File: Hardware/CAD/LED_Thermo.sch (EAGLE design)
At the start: 41 parts, among them IC1 MEGA48/88/168-AU, IC2 MAX481CSA, J1 USB_Micro, Q2 KERAMIKRESONATOR_CSTCC_16MHZ

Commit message: Sicherung eingefuegt, Gerberdateien aktualisiert
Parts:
- added F1: FUSE, fuse:FUSE
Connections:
- new net N$4: F1.1, J1.VBUS
- net VCC: now also F1.2; no longer J1.VBUS
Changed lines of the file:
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@@
 <setting verticaltext="up"/>
 </settings>
-<grid distance="25" unitdist="mil" unit="mil" style="lines" multiple="1" display="no" altdistance="5" altunitdist="mil" altunit="mil"/>
+<grid distance="50" unitdist="mil" unit="mil" style="lines" multiple="1" display="no" altdistance="5" altunitdist="mil" altunit="mil"/>
 <layers>
-<layer number="1" name="Top" color="4" fill="1" visible="yes" active="no"/>
-<layer number="2" name="Route2" color="1" fill="3" visible="yes" active="no"/>
-<layer number="3" name="Route3" color="4" fill="3" visible="yes" active="no"/>
-<layer number="4" name="Route4" color="1" fill="4" visible="yes" active="no"/>
-<layer number="5" name="Route5" color="4" fill="4" visible="yes" active="no"/>
-<layer number="6" name="Route6" color="1" fill="8" visible="yes" active="no"/>
-<layer number="7" name="Route7" color="4" fill="8" visible="yes" active="no"/>
-<layer number="8" name="Route8" color="1" fill="2" visible="yes" active="no"/>
-<layer number="9" name="Route9" color="4" fill="2" visible="yes" active="no"/>
-<layer number="10" name="Route10" color="1" fill="7" visible="yes" active="no"/>
-<layer number="11" name="Route11" color="4" fill="7" visible="yes" active="no"/>
-<layer number="12" name="Route12" color="1" fill="5" visible="yes" active="no"/>
-<layer number="13" name="Route13" color="4" fill="5" visible="yes" active="no"/>
-<layer number="14" name="Route14" color="1" fill="6" visible="yes" active="no"/>
-<layer number="15" name="Route15" color="4" fill="6" visible="yes" active="no"/>
-<layer number="16" name="Bottom" color="1" fill="1" visible="yes" active="no"/>
-<layer number="17" name="Pads" color="2" fill="1" visible="yes" active="no"/>
-<layer number="18" name="Vias" color="2" fill="1" visible="yes" active="no"/>
-<layer number="19" name="Unrouted" color="6" fill="1" visible="yes" active="no"/>
-<layer number="20" name="Dimension" color="15" fill="1" visible="yes" active="no"/>
-<layer number="21" name="tPlace" color="7" fill="1" visible="yes" active="no"/>
-<layer number="22" name="bPlace" color="7" fill="1" visible="yes" active="no"/>
-<layer number="23" name="tOrigins" color="15" fill="1" visible="yes" active="no"/>
-<layer number="24" name="bOrigins" color="15" fill="1" visible="yes" active="no"/>
-<layer number="25" name="tNames" color="7" fill="1" visible="yes" active="no"/>
-<layer number="26" name="bNames" color="7" fill="1" visible="yes" active="no"/>
-<layer number="27" name="tValues" color="7" fill="1" visible="yes" active="no"/>
-<layer number="28" name="bValues" color="7" fill="1" visible="yes" active="no"/>
+<layer number="1" name="Top" color="4" fill="1" visible="no" active="no"/>
+<layer number="2" name="Route2" color="1" fill="3" visible="no" active="no"/>
+<layer number="3" name="Route3" color="4" fill="3" visible="no" active="no"/>
+<layer number="4" name="Route4" color="1" fill="4" visible="no" active="no"/>
+<layer number="5" name="Route5" color="4" fill="4" visible="no" active="no"/>
+<layer number="6" name="Route6" color="1" fill="8" visible="no" active="no"/>
+<layer number="7" name="Route7" color="4" fill="8" visible="no" active="no"/>
+<layer number="8" name="Route8" color="1" fill="2" visible="no" active="no"/>
+<layer number="9" name="Route9" color="4" fill="2" visible="no" active="no"/>
+<layer number="10" name="Route10" color="1" fill="7" visible="no" active="no"/>
+<layer number="11" name="Route11" color="4" fill="7" visible="no" active="no"/>
+<layer number="12" name="Route12" color="1" fill="5" visible="no" active="no"/>
+<layer number="13" name="Route13" color="4" fill="5" visible="no" active="no"/>
+<layer number="14" name="Route14" color="1" fill="6" visible="no" active="no"/>
+<layer number="15" name="Route15" color="4" fill="6" visible="no" active="no"/>
+<layer number="16" name="Bottom" color="1" fill="1" visible="no" active="no"/>
+<layer number="17" name="Pads" color="2" fill="1" visible="no" active="no"/>
+<layer number="18" name="Vias" color="2" fill="1" visible="no" active="no"/>
+<layer number="19" name="Unrouted" color="6" fill="1" visible="no" active="no"/>
+<layer number="20" name="Dimension" color="15" fill="1" visible="no" active="no"/>
+<layer number="21" name="tPlace" color="7" fill="1" visible="no" active="no"/>
+<layer number="22" name="bPlace" color="7" fill="1" visible="no" active="no"/>
+<layer number="23" name="tOrigins" color="15" fill="1" visible="no" active="no"/>
+<layer number="24" name="bOrigins" color="15" fill="1" visible="no" active="no"/>
+<layer number="25" name="tNames" color="7" fill="1" visible="no" active="no"/>
+<layer number="26" name="bNames" color="7" fill="1" visible="no" active="no"/>
+<layer number="27" name="tValues" color="7" fill="1" visible="no" active="no"/>
+<layer number="28" name="bValues" color="7" fill="1" visible="no" active="no"/>
 <layer number="29" name="tStop" color="7" fill="3" visible="no" active="no"/>
 <layer number="30" name="bStop" color="7" fill="6" visible="no" active="no"/>
@@
 <layer number="35" name="tGlue" color="7" fill="4" visible="no" active="no"/>
 <layer number="36" name="bGlue" color="7" fill="5" visible="no" active="no"/>
-<layer number="37" name="tTest" color="7" fill="1" visible="yes" active="no"/>
-<layer number="38" name="bTest" color="7" fill="1" visible="yes" active="no"/>
+<layer number="37" name="tTest" color="7" fill="1" visible="no" active="no"/>
+<layer number="38" name="bTest" color="7" fill="1" visible="no" active="no"/>
 <layer number="39" name="tKeepout" color="4" fill="11" visible="no" active="no"/>
 <layer number="40" name="bKeepout" color="1" fill="11" visible="no" active="no"/>
@@
 <layer number="44" name="Drills" color="7" fill="1" visible="no" active="no"/>
 <layer number="45" name="Holes" color="7" fill="1" visible="no" active="no"/>
-<layer number="46" name="Milling" color="3" fill="1" visible="yes" active="no"/>
-<layer number="47" name="Measures" color="7" fill="1" visible="yes" active="no"/>
-<layer number="48" name="Document" color="7" fill="1" visible="yes" active="no"/>
-<layer number="49" name="Reference" color="7" fill="1" visible="yes" active="no"/>
-<layer number="50" name="dxf" color="7" fill="1" visible="yes" active="no"/>
-<layer number="51" name="tDocu" color="7" fill="1" visible="yes" active="no"/>
-<layer number="52" name="bDocu" color="7" fill="1" visible="yes" active="no"/>
-<layer number="53" name="tGND_GNDA" color="7" fill="9" visible="yes" active="no"/>
-<layer number="54" name="bGND_GNDA" color="1" fill="9" visible="yes" active="no"/>
-<layer number="56" name="wert" color="7" fill="1" visible="yes" active="no"/>
-<layer number="59" name="Invisible" color="7" fill="1" visible="yes" active="no"/>
-<layer number="61" name="stand" color="7" fill="1" visible="yes" active="no"/>
+<layer number="46" name="Milling" color="3" fill="1" visible="no" active="no"/>
+<layer number="47" name="Measures" color="7" fill="1" visible="no" active="no"/>
+<layer number="48" name="Document" color="7" fill="1" visible="no" active="no"/>
+<layer number="49" name="Reference" color="7" fill="1" visible="no" active="no"/>
+<layer number="50" name="dxf" color="7" fill="1" visible="no" active="no"/>
+<layer number="51" name="tDocu" color="7" fill="1" visible="no" active="no"/>
+<layer number="52" name="bDocu" color="7" fill="1" visible="no" active="no"/>
+<layer number="53" name="tGND_GNDA" color="7" fill="9" visible="no" active="no"/>
+<layer number="54" name="bGND_GNDA" color="1" fill="9" visible="no" active="no"/>
+<layer number="56" name="wert" color="7" fill="1" visible="no" active="no"/>
+<layer number="59" name="Invisible" color="7" fill="1" visible="no" active="no"/>
+<layer number="61" name="stand" color="7" fill="1" visible="no" active="no"/>
 <layer number="90" name="Modules" color="7" fill="1" visible="yes" active="yes"/>
 <layer number="91" name="Nets" color="2" fill="1" visible="yes" active="yes"/>
@@
 <part name="J1" library="InputOutputIO (rev19b)" deviceset="614105150721" device="" value="USB_Micro"/>
 <part name="GND3" library="supply1" deviceset="GND" device=""/>
+<part name="F1" library="fuse" deviceset="FUSE" device=""/>
 </parts>
 <sheets>
@@
 <instance part="J1" gate="G$1" x="20.32" y="86.36" rot="R180"/>
 <instance part="GND3" gate="1" x="27.94" y="69.85"/>
+<instance part="F1" gate="G$1" x="38.1" y="93.98"/>
 </instances>
 <busses>
@@
 <pinref part="IC2" gate="P" pin="VCC"/>
 <pinref part="R3" gate="G$1" pin="1"/>
-<wire x1="71.12" y1="119.38" x2="71.12" y2="91.44" width="0.1524" layer="91"/>
-<pinref part="J1" gate="G$1" pin="VBUS"/>
-<wire x1="71.12" y1="91.44" x2="27.94" y2="91.44" width="0.1524" layer="91"/>
+<wire x1="71.12" y1="119.38" x2="71.12" y2="93.98" width="0.1524" layer="91"/>
+<pinref part="F1" gate="G$1" pin="2"/>
+<wire x1="43.18" y1="93.98" x2="71.12" y2="93.98" width="0.1524" layer="91"/>
 </segment>
 </net>
@@
 </segment>
 </net>
+<net name="N$4" class="0">
+<segment>
+<pinref part="J1" gate="G$1" pin="VBUS"/>
+<pinref part="F1" gate="G$1" pin="1"/>
+<wire x1="27.94" y1="91.44" x2="33.02" y2="91.44" width="0.1524" layer="91"/>
+<wire x1="33.02" y1="91.44" x2="33.02" y2="93.98" width="0.1524" layer="91"/>
+</segment>
+</net>

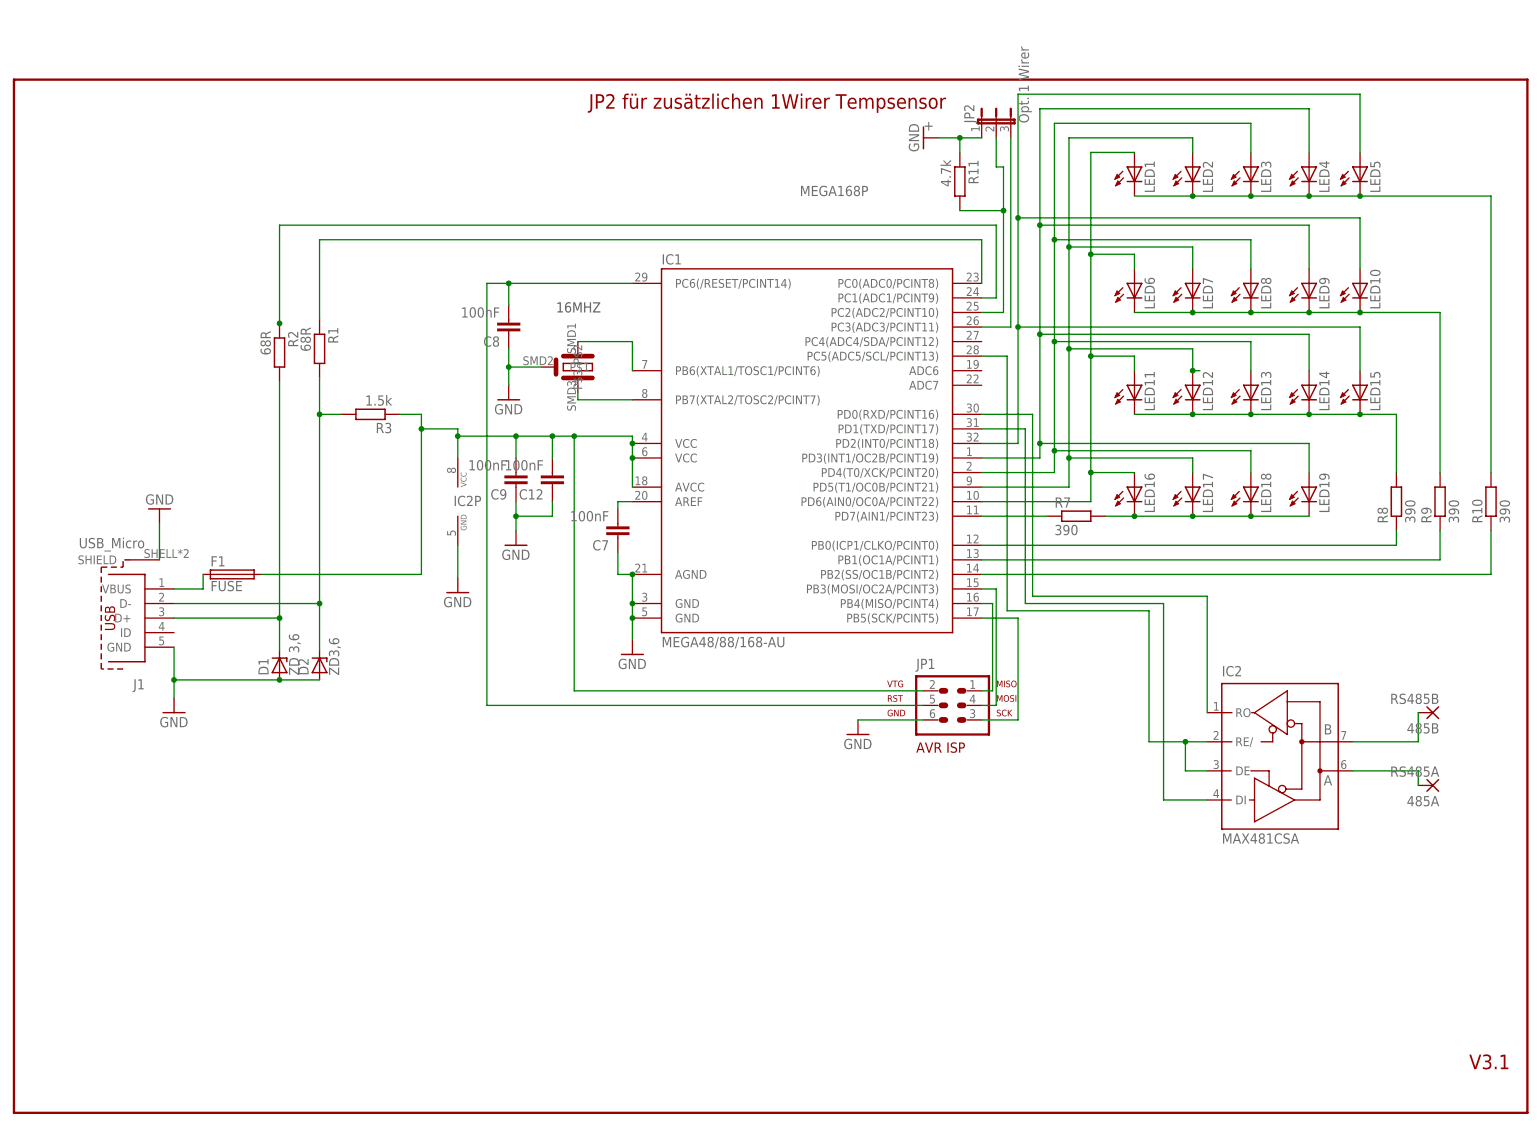
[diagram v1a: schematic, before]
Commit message: Taster eingefuegt, Gerberdateien ueberarbeitet
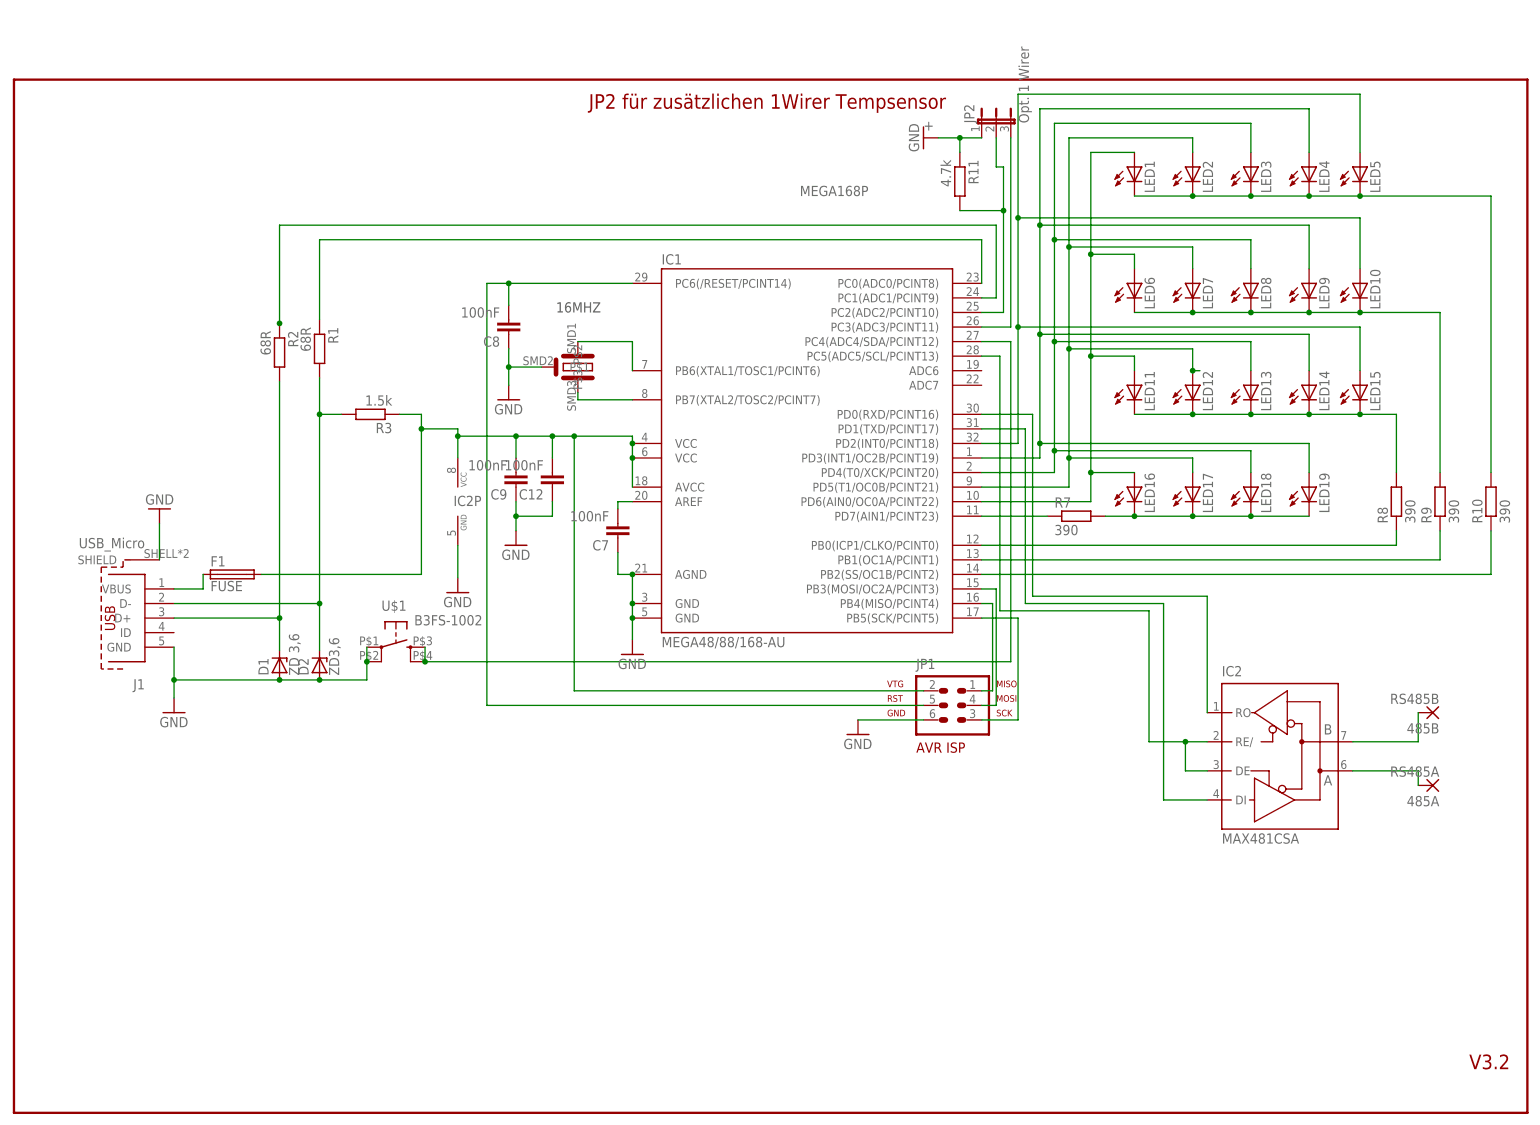
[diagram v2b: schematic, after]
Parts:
- added U$1: B3FS-1002, switch-omron:B3FS-10XX
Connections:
- new net N$6: IC1.PC4(ADC4/SDA/PCINT12), U$1.S, U$1.S1
- net GND: now also U$1.P, U$1.P1
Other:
- note added: "V3.2"
- note removed: "V3.1"
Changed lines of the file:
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@@
 <setting verticaltext="up"/>
 </settings>
-<grid distance="50" unitdist="mil" unit="mil" style="lines" multiple="1" display="no" altdistance="5" altunitdist="mil" altunit="mil"/>
+<grid distance="25" unitdist="mil" unit="mil" style="lines" multiple="1" display="no" altdistance="5" altunitdist="mil" altunit="mil"/>
 <layers>
 <layer number="1" name="Top" color="4" fill="1" visible="no" active="no"/>
@@
 <part name="GND3" library="supply1" deviceset="GND" device=""/>
 <part name="F1" library="fuse" deviceset="FUSE" device=""/>
+<part name="U$1" library="switch-omron" deviceset="B3FS-10XX" device="" value="B3FS-1002"/>
 </parts>
 <sheets>
@@
 <text x="137.16" y="160.02" size="1.778" layer="96">MEGA168P</text>
 <text x="158.75" y="171.45" size="1.778" layer="96">+</text>
-<text x="254" y="7.62" size="2.54" layer="94">V3.1</text>
+<text x="254" y="7.62" size="2.54" layer="94">V3.2</text>
 <text x="100.33" y="175.26" size="2.54" layer="94">JP2 für zusätzlichen 1Wirer Tempsensor</text>
 <text x="94.615" y="139.7" size="1.778" layer="97">16MHZ</text>
@@
 <instance part="GND3" gate="1" x="27.94" y="69.85"/>
 <instance part="F1" gate="G$1" x="38.1" y="93.98"/>
+<instance part="U$1" gate="G$1" x="66.675" y="81.28" rot="R270"/>
 </instances>
 <busses>
@@
 <junction x="27.94" y="75.565"/>
 <pinref part="D2" gate="G$1" pin="A"/>
+<junction x="46.355" y="75.565"/>
+<pinref part="U$1" gate="G$1" pin="P1"/>
 <wire x1="53.34" y1="75.565" x2="46.355" y2="75.565" width="0.1524" layer="91"/>
-<junction x="46.355" y="75.565"/>
+<wire x1="53.34" y1="75.565" x2="61.595" y2="75.565" width="0.1524" layer="91"/>
+<wire x1="61.595" y1="75.565" x2="61.595" y2="78.74" width="0.1524" layer="91"/>
+<pinref part="U$1" gate="G$1" pin="P"/>
+<wire x1="61.595" y1="78.74" x2="61.595" y2="81.28" width="0.1524" layer="91"/>
+<junction x="61.595" y="78.74"/>
+<junction x="53.34" y="75.565"/>
 </segment>
 </net>
@@
 <net name="N$29" class="0">
 <segment>
-<wire x1="173.355" y1="87.63" x2="198.12" y2="87.63" width="0.1524" layer="91"/>
+<wire x1="172.085" y1="87.63" x2="198.12" y2="87.63" width="0.1524" layer="91"/>
 <wire x1="198.12" y1="87.63" x2="198.12" y2="64.77" width="0.1524" layer="91"/>
 <wire x1="198.12" y1="64.77" x2="204.47" y2="64.77" width="0.1524" layer="91"/>
@@
 <wire x1="208.28" y1="59.69" x2="204.47" y2="59.69" width="0.1524" layer="91"/>
 <wire x1="204.47" y1="59.69" x2="204.47" y2="64.77" width="0.1524" layer="91"/>
-<wire x1="168.91" y1="132.08" x2="173.355" y2="132.08" width="0.1524" layer="91"/>
-<wire x1="173.355" y1="132.08" x2="173.355" y2="87.63" width="0.1524" layer="91"/>
+<wire x1="168.91" y1="132.08" x2="172.085" y2="132.08" width="0.1524" layer="91"/>
+<wire x1="172.085" y1="132.08" x2="172.085" y2="87.63" width="0.1524" layer="91"/>
 <junction x="204.47" y="64.77"/>
 <pinref part="IC2" gate="G$1" pin="RE/"/>
@@
 </segment>
 </net>
+<net name="N$6" class="0">
+<segment>
+<pinref part="IC1" gate="1" pin="PC4(ADC4/SDA/PCINT12)"/>
+<wire x1="168.91" y1="134.62" x2="173.99" y2="134.62" width="0.1524" layer="91"/>
+<wire x1="173.99" y1="134.62" x2="173.99" y2="78.74" width="0.1524" layer="91"/>
+<pinref part="U$1" gate="G$1" pin="S1"/>
+<wire x1="173.99" y1="78.74" x2="71.755" y2="78.74" width="0.1524" layer="91"/>
+<pinref part="U$1" gate="G$1" pin="S"/>
+<wire x1="71.755" y1="78.74" x2="71.755" y2="81.28" width="0.1524" layer="91"/>
+<junction x="71.755" y="78.74"/>
+</segment>
+</net>

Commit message: USB-Schutzschaltung,12MHZ Quarz integriert,Layout + Loetstopmake optimiert
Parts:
- removed D1: ZD 3,6, diode:ZENER-DIODESOT23
- removed D2: ZD3,6, diode:ZENER-DIODESOT23
- removed J1: USB_Micro, InputOutputIO (rev19b):614105150721
- removed Q2: KERAMIKRESONATOR_CSTCC_16MHZ, atmel:KERAMIKRESONATOR_CSTCC
- removed U$1: B3FS-1002, switch-omron:B3FS-10XX
- added C1, C2: 22pF, rcl:C-EUC0805
- added IC3: IP4220CZ6, IP4220CZ6:IP4220CZ6
- added JP3: USB_Micro, InputOutputIO (rev19b):614105150721
- added Q1: 12MHZ, crystal:CRYSTALHC18U-V
- added SW1: B3FS-1002, switch-omron:B3FS-10XX
- 485A: value RS485A -> (+)
- 485B: value RS485B -> B(-)
- IC1: value MEGA48/88/168-AU -> MEGA68-AU
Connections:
- net GND: now also C1.1, C2.1, IC3.GND, JP3.GND, JP3.SHIELD, SW1.P, SW1.P1; no longer D1.A, D2.A, J1.GND, J1.SHIELD, Q2.P$1, U$1.P, U$1.P1
- net N$24: now also C1.2, Q1.2; no longer Q2.P$3
- net N$25: now also C2.2, Q1.1; no longer Q2.P$2
- net N$4: now also JP3.VBUS; no longer J1.VBUS
- net N$6: now also SW1.S, SW1.S1; no longer U$1.S, U$1.S1
- net N$7: now also IC3.I/O_4, JP3.D+; no longer D1.C, J1.D+
- net N$8: now also IC3.I/O_2, JP3.D-; no longer D2.C, J1.D-
- net VCC: now also IC3.VP
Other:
- note added: "V3.3"
- note removed: "16MHZ"
- note removed: "V3.2"
- moved on the sheet: C8, F1, R1, R2, R3
